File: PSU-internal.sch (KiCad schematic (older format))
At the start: 56 parts, among them Q1 BD241A, Q2 BD241A, Q3 BD242, U1 OPA27, U2 OPA27, U3 OPA27, U4 2N6507, U5 2N6507, U6 2N6507, U7 REF02, U8 2N6507, U9 OPA27

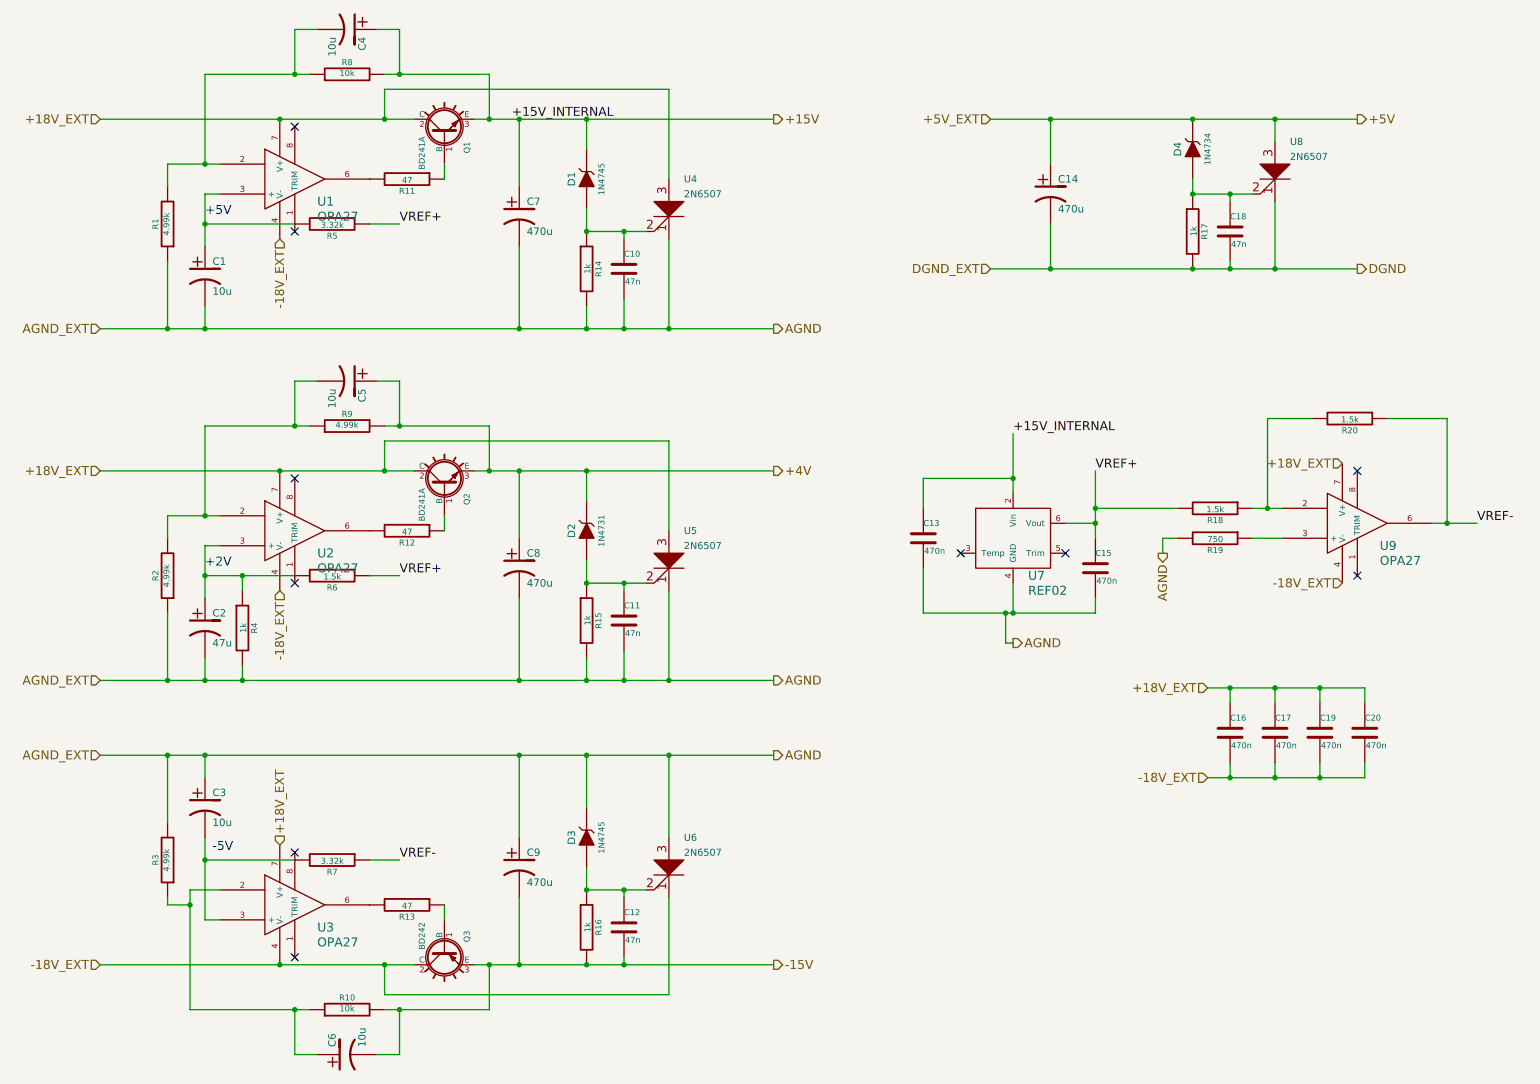
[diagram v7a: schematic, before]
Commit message: First complete version.   * Added 10uF decoupling capacitors to the start of each signal processing section.   * Completed routing.  A few -18 V nets remain unrouted; these will be wired in.
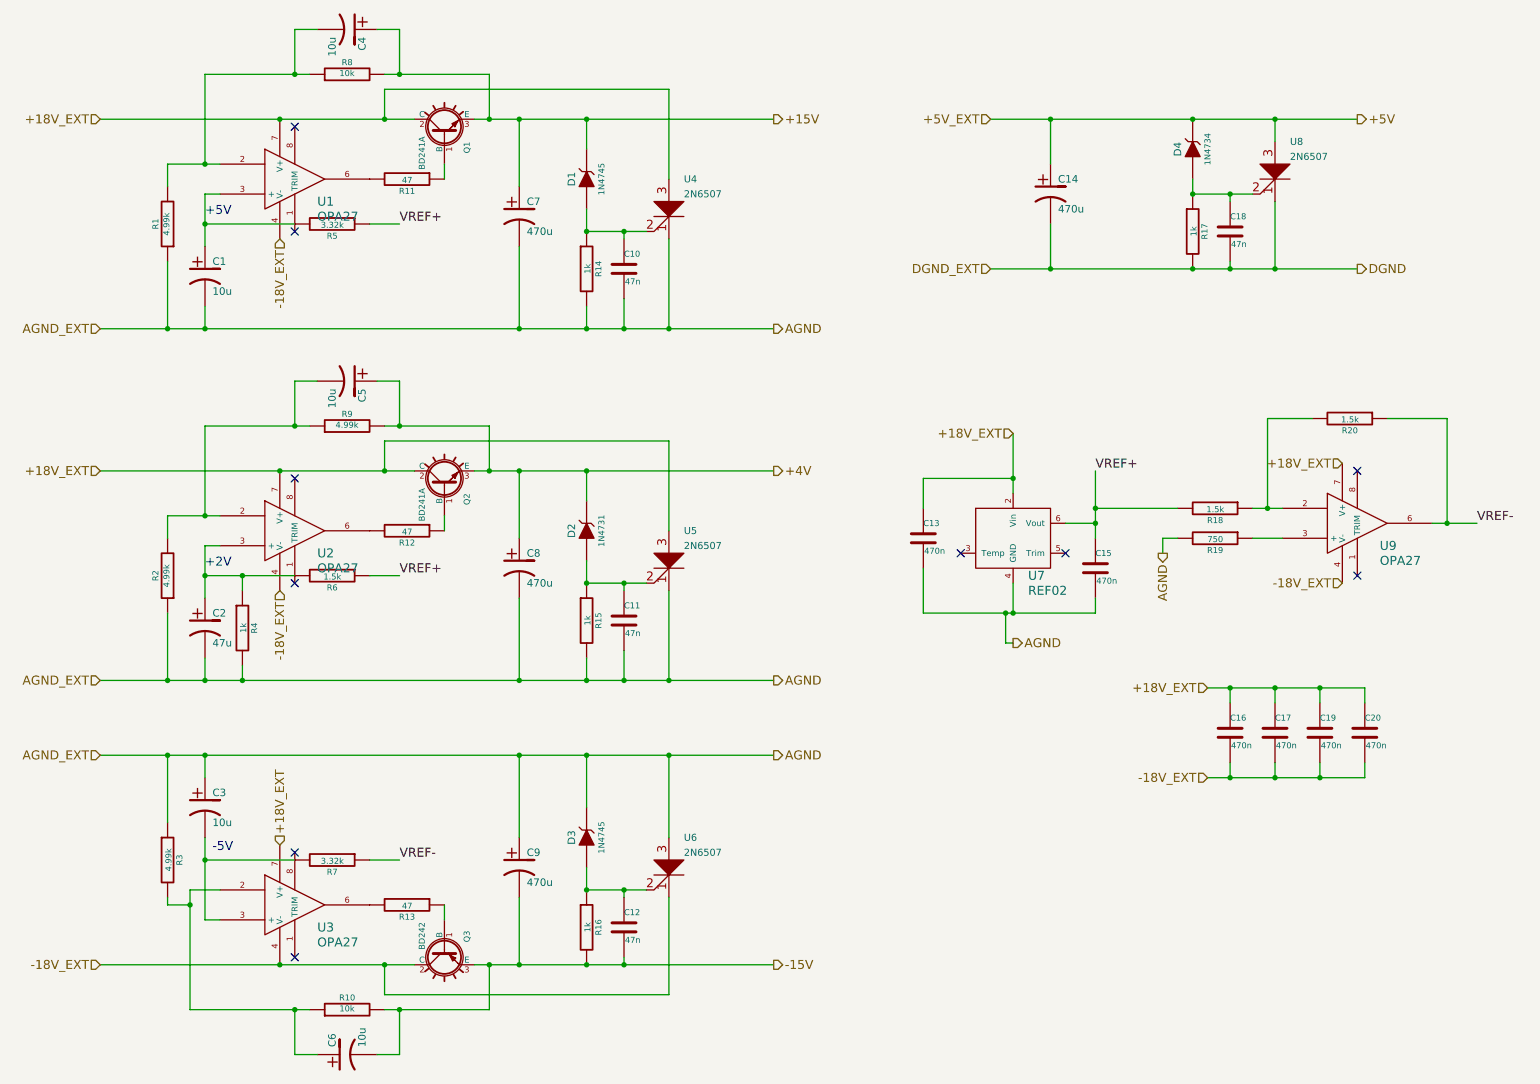
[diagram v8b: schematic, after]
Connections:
- net +15V: no longer C13.1, U7.2 (Vin)
- net +18V_EXT: now also C13.1, U7.2 (Vin)
- net AGND: now also R3.1; no longer R3.2
- net at C6.1, R10.1, U3.2: now also R3.2; no longer R3.1
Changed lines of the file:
@@
 Text Label 10550 4000 0    60   ~ 0
 VREF-
-Text Label 4100 1300 0    60   ~ 0
-+15V_INTERNAL
-Text Label 7450 3400 0    60   ~ 0
-+15V_INTERNAL
 Text Label 3350 4350 0    60   ~ 0
 VREF+
@@
 F 4 "4.99KXBK-ND" V 1800 6250 60  0001 C CNN "DigiKey"
 	1    1800 6250
-	-1   0    0    1
+	1    0    0    -1
 $EndComp
 $Comp
@@
 NoConn ~ 9750 3650
 NoConn ~ 9750 4350
+Text HLabel 7450 3400 0    60   Input ~ 0
++18V_EXT
 $EndSCHEMATC
